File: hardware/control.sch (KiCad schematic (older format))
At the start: 2 parts

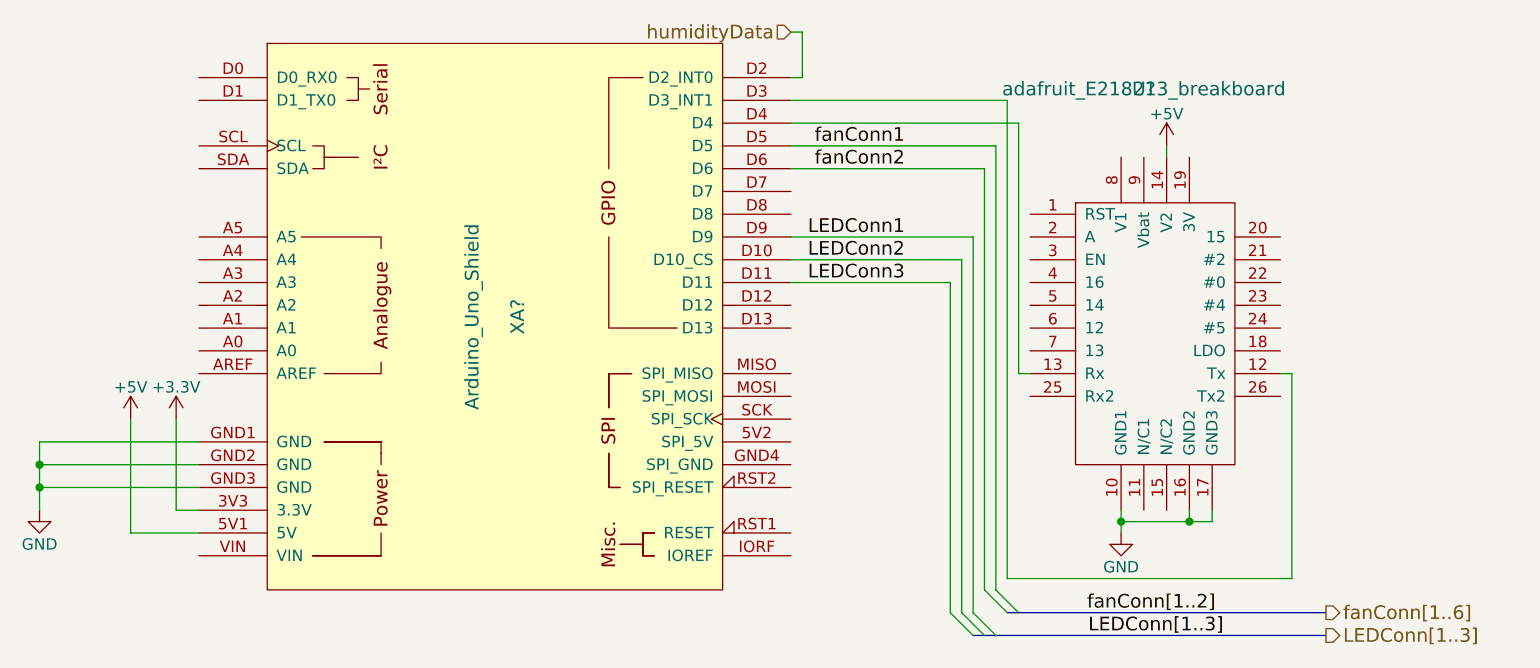
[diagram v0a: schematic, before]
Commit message: sheets are named, global circuit is done.
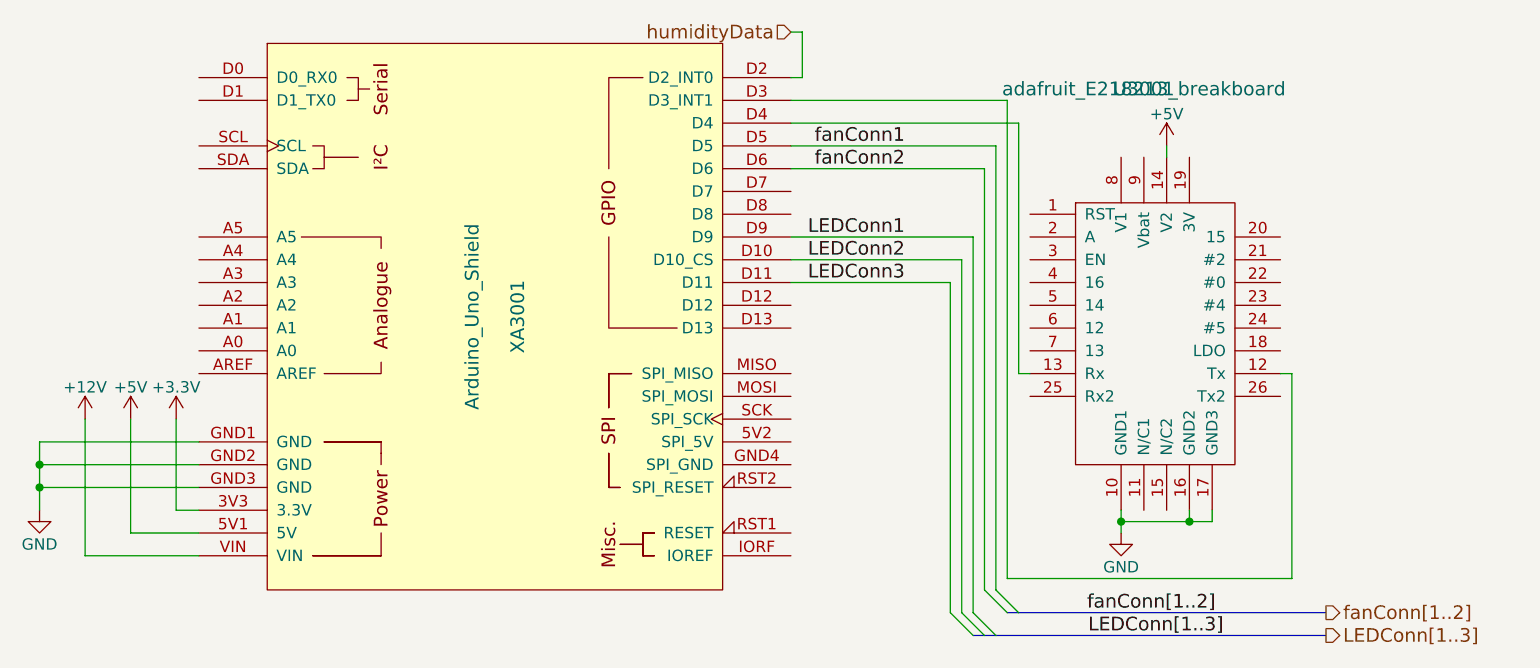
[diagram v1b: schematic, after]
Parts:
- gave numbers to parts that had none: 2
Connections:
- net +12V: now reaches XA3001.VIN
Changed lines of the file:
@@
 LIBS:contrib
 LIBS:valves
+LIBS:arduino
+LIBS:ESP8266
 LIBS:LDD1500H
-LIBS:ESP8266
-LIBS:arduino
-LIBS:control-cache
+LIBS:jardinio-cache
 EELAYER 25 0
 EELAYER END
 $Descr A4 11693 8268
 encoding utf-8
-Sheet 1 1
-Title ""
-Date ""
-Rev ""
-Comp ""
+Sheet 1 5
+Title "jardinIO circuit"
+Date "2018-04-18"
+Rev "0"
+Comp "Cedille"
 Comment1 ""
 Comment2 ""
@@
 $EndDescr
 $Comp
-L Arduino_Uno_Shield XA?
+L Arduino_Uno_Shield XA3001
 U 1 1 5AA1EDD2
 P 2750 2000
-F 0 "XA?" V 2850 2000 60  0000 C CNN
+F 0 "XA3001" V 2850 2000 60  0000 C CNN
 F 1 "Arduino_Uno_Shield" V 2650 2000 60  0000 C CNN
 F 2 "" H 4550 5750 60  0001 C CNN
@@
 $EndComp
 $Comp
-L GND #PWR?
+L GND #PWR06
 U 1 1 5AA88684
 P 750 2850
-F 0 "#PWR?" H 750 2600 50  0001 C CNN
+F 0 "#PWR06" H 750 2600 50  0001 C CNN
 F 1 "GND" H 750 2700 50  0000 C CNN
 F 2 "" H 750 2850 50  0000 C CNN
@@
 $EndComp
 $Comp
-L +3.3V #PWR?
+L +3.3V #PWR07
 U 1 1 5AA88986
 P 1350 2450
-F 0 "#PWR?" H 1350 2300 50  0001 C CNN
+F 0 "#PWR07" H 1350 2300 50  0001 C CNN
 F 1 "+3.3V" H 1350 2590 50  0000 C CNN
 F 2 "" H 1350 2450 50  0000 C CNN
@@
 $EndComp
 $Comp
-L +5V #PWR?
+L +5V #PWR08
 U 1 1 5AA8899E
 P 1150 2450
-F 0 "#PWR?" H 1150 2300 50  0001 C CNN
+F 0 "#PWR08" H 1150 2300 50  0001 C CNN
 F 1 "+5V" H 1150 2590 50  0000 C CNN
 F 2 "" H 1150 2450 50  0000 C CNN
@@
 $EndComp
 $Comp
-L adafruit_E218213_breakboard U?
+L adafruit_E218213_breakboard U3001
 U 1 1 5AB05516
 P 3250 3150
-F 0 "U?" H 5600 5300 60  0000 C CNN
+F 0 "U3001" H 5600 5300 60  0000 C CNN
 F 1 "adafruit_E218213_breakboard" H 5600 5300 60  0000 C CNN
 F 2 "" H 5600 5300 60  0000 C CNN
@@
 $EndComp
 $Comp
-L GND #PWR?
+L GND #PWR09
 U 1 1 5AB0561B
 P 5500 2950
-F 0 "#PWR?" H 5500 2700 50  0001 C CNN
+F 0 "#PWR09" H 5500 2700 50  0001 C CNN
 F 1 "GND" H 5500 2800 50  0000 C CNN
 F 2 "" H 5500 2950 50  0000 C CNN
@@
 $EndComp
 $Comp
-L +5V #PWR?
+L +5V #PWR010
 U 1 1 5AB056CD
 P 5700 1250
-F 0 "#PWR?" H 5700 1100 50  0001 C CNN
+F 0 "#PWR010" H 5700 1100 50  0001 C CNN
 F 1 "+5V" H 5700 1390 50  0000 C CNN
 F 2 "" H 5700 1250 50  0000 C CNN
@@
 	1    0    0    -1
 $EndComp
-Wire Wire Line
-	1450 2550 750  2550
-Wire Wire Line
-	750  2550 750  2850
-Wire Wire Line
-	1450 2650 750  2650
-Connection ~ 750  2650
-Wire Wire Line
-	1450 2750 750  2750
-Connection ~ 750  2750
-Wire Wire Line
-	1350 2450 1350 2850
-Wire Wire Line
-	1350 2850 1450 2850
-Wire Wire Line
-	1150 2450 1150 2950
-Wire Wire Line
-	1150 2950 1450 2950
-Wire Wire Line
-	5900 2850 5900 2900
-Wire Wire Line
-	5900 2900 5500 2900
-Wire Wire Line
-	5500 2850 5500 2950
-Connection ~ 5500 2900
-Wire Wire Line
-	5800 2850 5800 2900
-Connection ~ 5800 2900
-Wire Wire Line
-	5700 1300 5700 1250
-Wire Wire Line
-	4050 1150 5050 1150
-Wire Wire Line
-	4050 1050 5000 1050
-Wire Wire Line
-	6250 3150 6250 2250
-Wire Wire Line
-	6250 2250 6200 2250
-Wire Wire Line
-	5100 2250 5050 2250
-Wire Wire Line
-	5050 2250 5050 1150
-Wire Wire Line
-	5000 1050 5000 3150
-Wire Wire Line
-	5000 3150 6250 3150
-Wire Wire Line
-	4050 1250 4950 1250
-Wire Wire Line
-	4950 1250 4950 3200
-Wire Wire Line
-	4050 1350 4900 1350
-Wire Wire Line
-	4900 1350 4900 3200
-Wire Wire Line
-	4050 1650 4850 1650
-Wire Wire Line
-	4850 1650 4850 3300
-Wire Wire Line
-	4050 1750 4800 1750
-Wire Wire Line
-	4800 1750 4800 3300
-Wire Wire Line
-	4050 1850 4750 1850
-Wire Wire Line
-	4750 1850 4750 3300
-Wire Bus Line
-	5000 3300 6400 3300
 Entry Wire Line
 	4750 3300 4850 3400
@@
 fanConn[1..2]
 Text HLabel 6400 3300 2    60   Output ~ 0
-fanConn[1..6]
+fanConn[1..2]
 Text HLabel 4050 750  0    60   Input ~ 0
 humidityData
-Wire Wire Line
-	4050 950  4100 950
-Wire Wire Line
-	4100 950  4100 750
-Wire Wire Line
-	4100 750  4050 750
 Text Label 4550 1250 2    60   ~ 0
 fanConn1
@@
 Text Label 4550 1850 2    60   ~ 0
 LEDConn3
-Wire Bus Line
-	4850 3400 6400 3400
 Text HLabel 6400 3400 2    60   Output ~ 0
 LEDConn[1..3]
 Text Label 5950 3400 2    60   ~ 0
 LEDConn[1..3]
+$Comp
+L +12V #PWR011
+U 1 1 5AD6AFCF
+P 950 2450
+F 0 "#PWR011" H 950 2300 50  0001 C CNN
+F 1 "+12V" H 950 2590 50  0000 C CNN
+F 2 "" H 950 2450 50  0000 C CNN
+F 3 "" H 950 2450 50  0000 C CNN
+	1    950  2450
+	1    0    0    -1
+$EndComp
+Wire Wire Line
+	1450 2550 750  2550
+Wire Wire Line
+	750  2550 750  2850
+Wire Wire Line
+	1450 2650 750  2650
+Connection ~ 750  2650
+Wire Wire Line
+	1450 2750 750  2750
+Connection ~ 750  2750
+Wire Wire Line
+	1350 2450 1350 2850
+Wire Wire Line
+	1350 2850 1450 2850
+Wire Wire Line
+	1150 2450 1150 2950
+Wire Wire Line
+	1150 2950 1450 2950
+Wire Wire Line
+	5900 2850 5900 2900
+Wire Wire Line
+	5900 2900 5500 2900
+Wire Wire Line
+	5500 2850 5500 2950
+Connection ~ 5500 2900
+Wire Wire Line
+	5800 2850 5800 2900
+Connection ~ 5800 2900
+Wire Wire Line
+	5700 1300 5700 1250
+Wire Wire Line
+	4050 1150 5050 1150
+Wire Wire Line
+	4050 1050 5000 1050
+Wire Wire Line
+	6250 3150 6250 2250
+Wire Wire Line
+	6250 2250 6200 2250
+Wire Wire Line
+	5100 2250 5050 2250
+Wire Wire Line
+	5050 2250 5050 1150
+Wire Wire Line
+	5000 1050 5000 3150
+Wire Wire Line
+	5000 3150 6250 3150
+Wire Wire Line
+	4050 1250 4950 1250
+Wire Wire Line
+	4950 1250 4950 3200
+Wire Wire Line
+	4050 1350 4900 1350
+Wire Wire Line
+	4900 1350 4900 3200
+Wire Wire Line
+	4050 1650 4850 1650
+Wire Wire Line
+	4850 1650 4850 3300
+Wire Wire Line
+	4050 1750 4800 1750
+Wire Wire Line
+	4800 1750 4800 3300
+Wire Wire Line
+	4050 1850 4750 1850
+Wire Wire Line
+	4750 1850 4750 3300
+Wire Bus Line
+	5000 3300 6400 3300
+Wire Wire Line
+	4050 950  4100 950
+Wire Wire Line
+	4100 950  4100 750
+Wire Wire Line
+	4100 750  4050 750
+Wire Bus Line
+	4850 3400 6400 3400
+Wire Wire Line
+	950  3050 1450 3050
+Wire Wire Line
+	950  3050 950  2450
 $EndSCHEMATC
